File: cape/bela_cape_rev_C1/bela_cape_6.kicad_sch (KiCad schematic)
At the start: 48 parts, among them IC3 ES9080Q, IC8 TL974, IC9 TL974, J12 Conn_01x03, J13 Conn_01x03, J14 Conn_01x03, J15 Conn_01x03

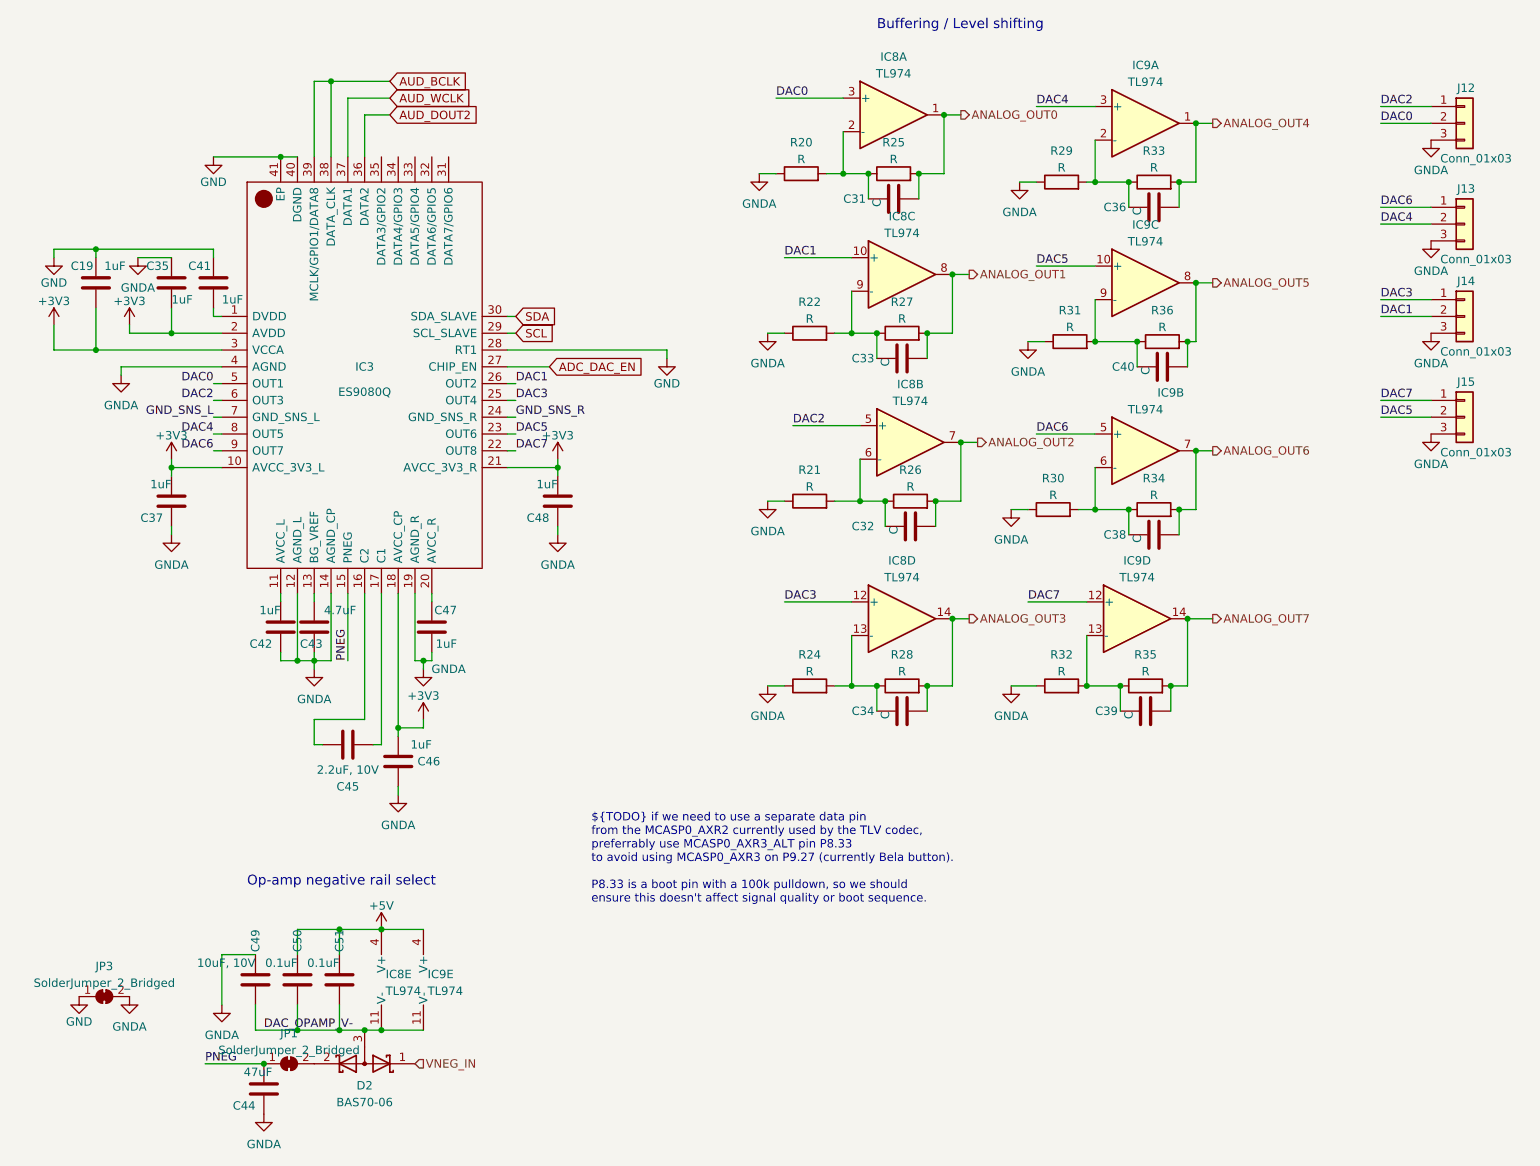
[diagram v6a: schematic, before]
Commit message: Bela cape C1: renumber components
(cherry picked from commit 6ebfe9c44bb7559ffb4c9dbd092e49803523e6a1)
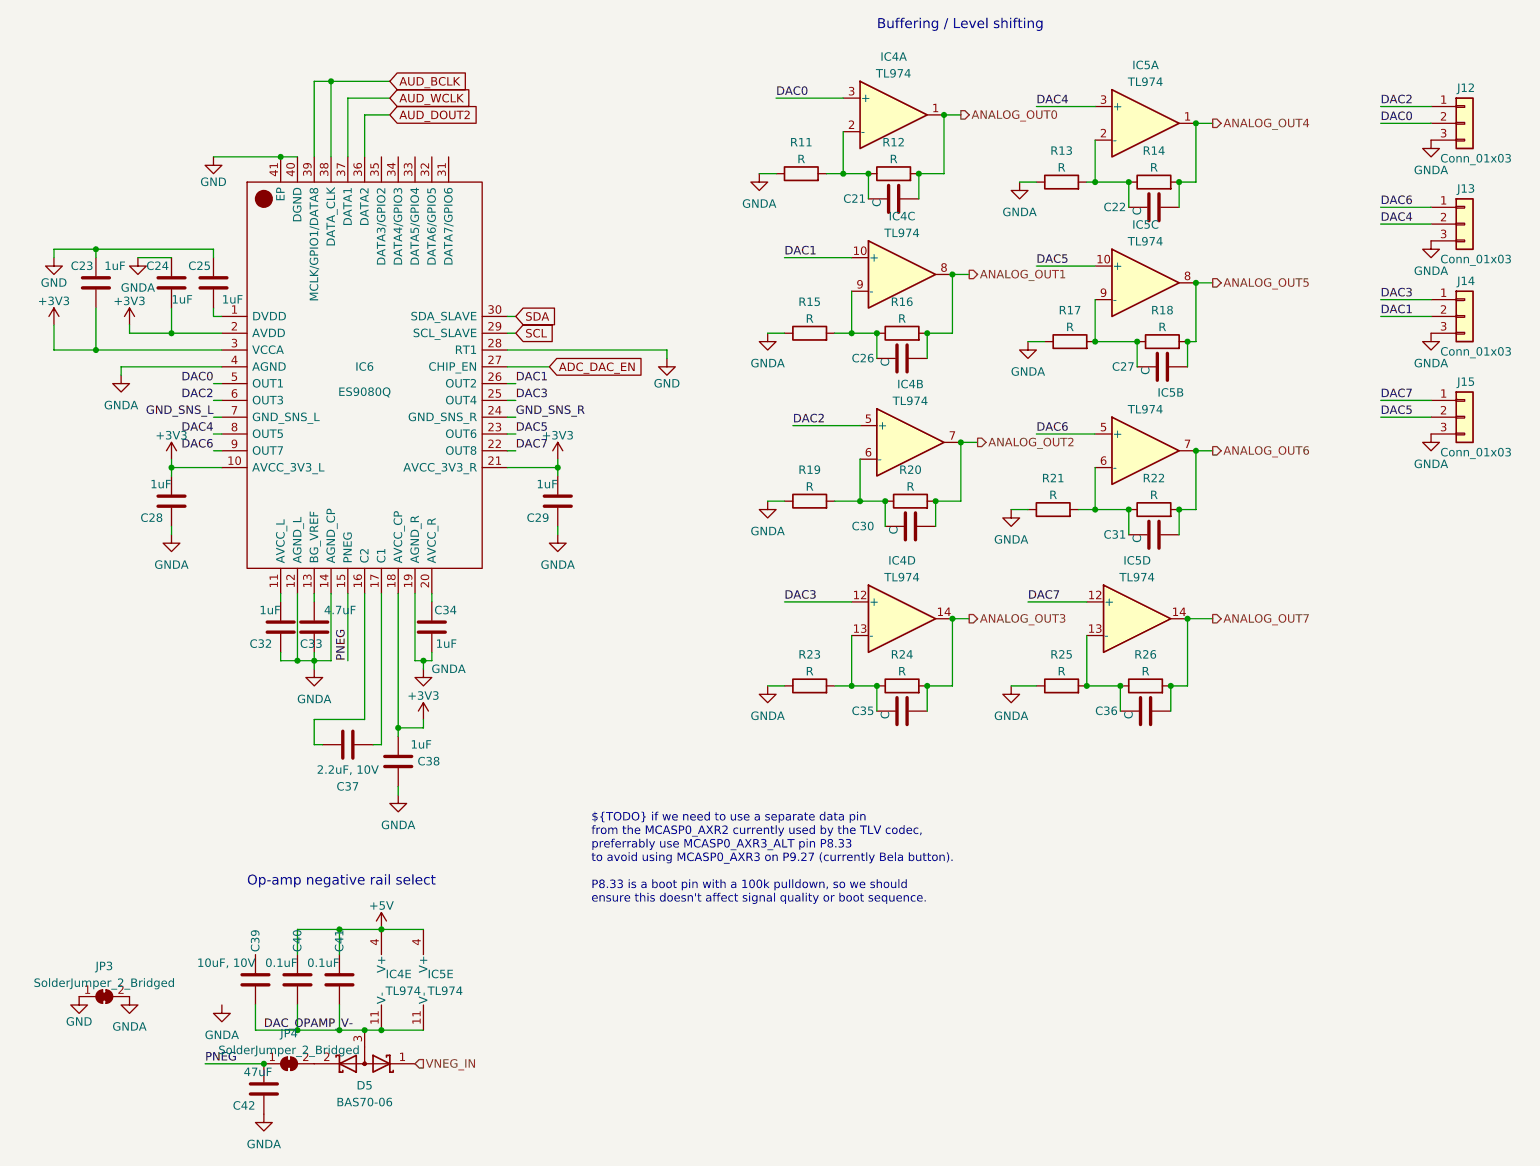
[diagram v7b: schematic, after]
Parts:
- renumbered C31 to C21, C36 to C22, C19 to C23, C35 to C24, C41 to C25, C33 to C26, C40 to C27, C37 to C28, C48 to C29, C32 to C30, C38 to C31, C42 to C32, C43 to C33, C47 to C34, C34 to C35, C39 to C36, C45 to C37, C46 to C38, C49 to C39, C50 to C40, C51 to C41, C44 to C42, D2 to D5, IC8 to IC4, IC9 to IC5, IC3 to IC6, JP1 to JP4, R20 to R11, R25 to R12, R29 to R13, R33 to R14, R22 to R15, R27 to R16, R31 to R17, R36 to R18, R21 to R19, R26 to R20, R30 to R21, R34 to R22, R24 to R23, R28 to R24, R32 to R25, R35 to R26
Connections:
- net GNDA: no longer C39.2

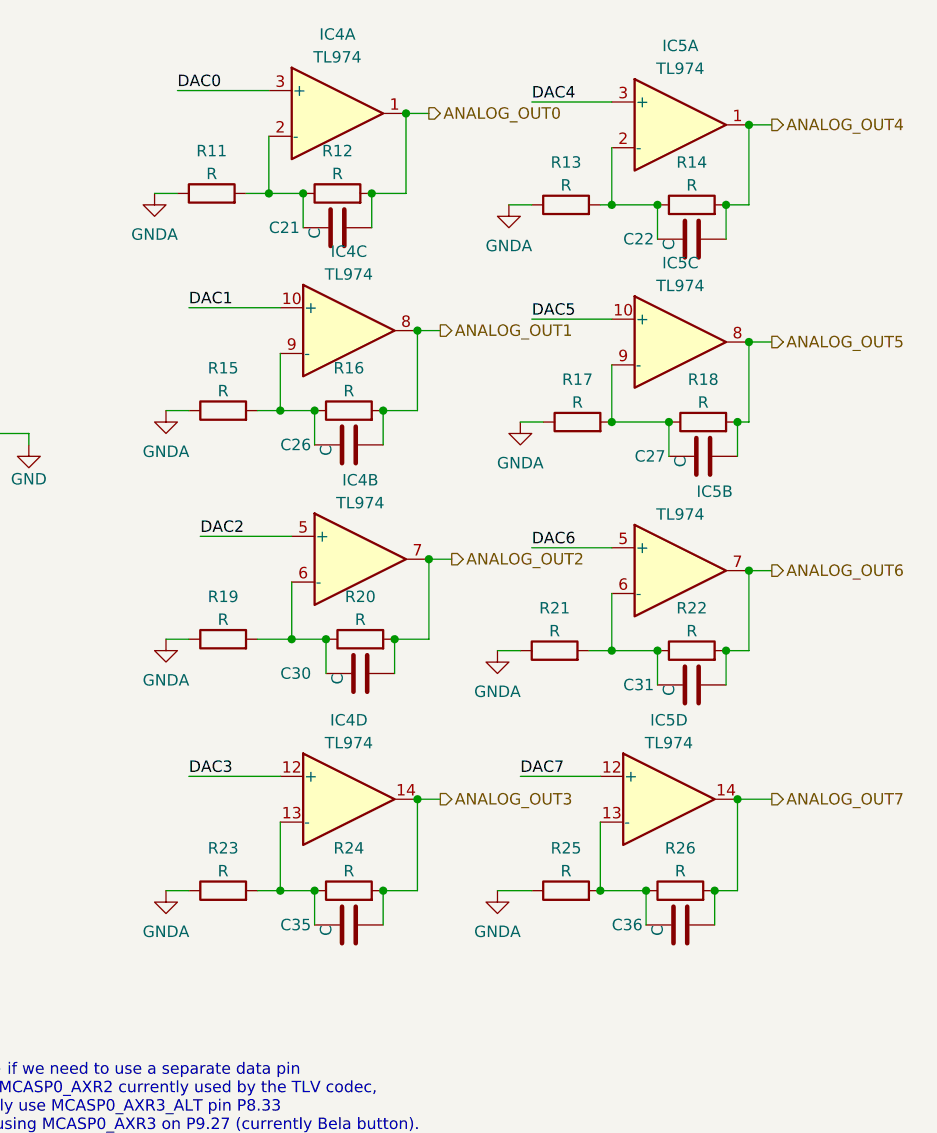
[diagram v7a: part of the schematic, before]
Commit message: First complete iteration of C1 cape layout
(cherry picked from commit 0ee733c70b42f416809330055e007cefcdb105fa)
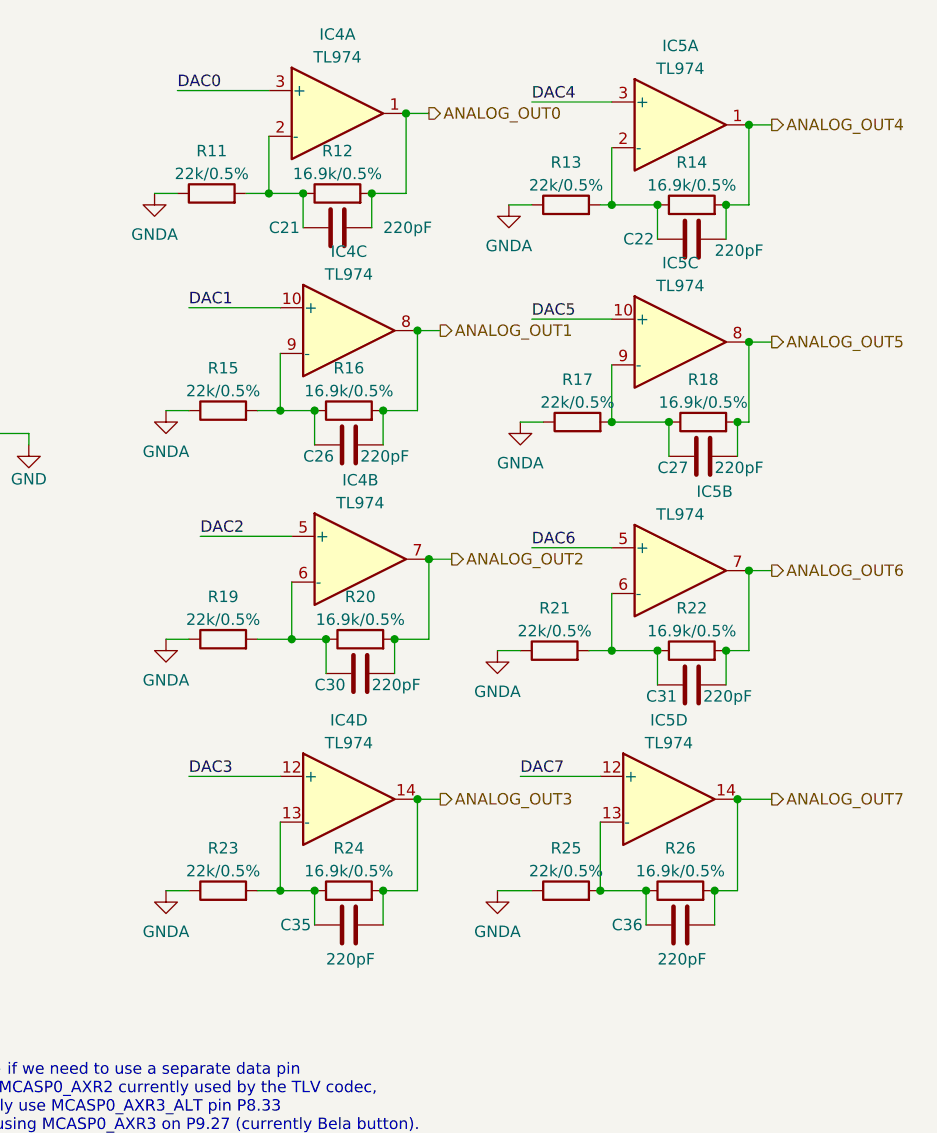
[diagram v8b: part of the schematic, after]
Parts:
- C21, C22, C26, C27, C30, C31, C35, C36: value C -> 220pF
- R11, R13, R15, R17, R19, R21, R23, R25: value R -> 22k/0.5%
- R12, R14, R16, R18, R20, R22, R24, R26: value R -> 16.9k/0.5%
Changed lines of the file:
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@@
   (symbol (lib_id "Device:C") (at 194.31 69.85 270) (unit 1)
     (in_bom yes) (on_board yes)
-    (property "Reference" "C27" (id 0) (at 186.69 69.85 90)
-      (effects (font (size 1.27 1.27)) (justify left))
-    )
-    (property "Value" "C" (id 1) (at 191.77 69.85 0)
+    (property "Reference" "C27" (id 0) (at 189.23 71.12 90)
+      (effects (font (size 1.27 1.27)) (justify left))
+    )
+    (property "Value" "220pF" (id 1) (at 195.58 71.12 90)
       (effects (font (size 1.27 1.27)) (justify left))
     )
@@
       (effects (font (size 1.27 1.27)) (justify left))
     )
-    (property "Value" "C" (id 1) (at 189.23 121.92 0)
+    (property "Value" "220pF" (id 1) (at 189.23 125.73 90)
       (effects (font (size 1.27 1.27)) (justify left))
     )
@@
     (in_bom yes) (on_board yes) (fields_autoplaced)
     (property "Reference" "R19" (id 0) (at 140.97 85.4542 90))
-    (property "Value" "R" (id 1) (at 140.97 87.9911 90))
+    (property "Value" "22k/0.5%" (id 1) (at 140.97 87.9911 90))
     (property "Footprint" "Resistor_SMD:R_0603_1608Metric" (id 2) (at 140.97 91.948 90)
       (effects (font (size 1.27 1.27)) hide)
@@
     (in_bom yes) (on_board yes) (fields_autoplaced)
     (property "Reference" "R26" (id 0) (at 191.77 113.3942 90))
-    (property "Value" "R" (id 1) (at 191.77 115.9311 90))
+    (property "Value" "16.9k/0.5%" (id 1) (at 191.77 115.9311 90))
     (property "Footprint" "Resistor_SMD:R_0603_1608Metric" (id 2) (at 191.77 119.888 90)
       (effects (font (size 1.27 1.27)) hide)
@@
     (in_bom yes) (on_board yes) (fields_autoplaced)
     (property "Reference" "R11" (id 0) (at 139.7 35.9242 90))
-    (property "Value" "R" (id 1) (at 139.7 38.4611 90))
+    (property "Value" "22k/0.5%" (id 1) (at 139.7 38.4611 90))
     (property "Footprint" "Resistor_SMD:R_0603_1608Metric" (id 2) (at 139.7 42.418 90)
       (effects (font (size 1.27 1.27)) hide)
@@
     (in_bom yes) (on_board yes) (fields_autoplaced)
     (property "Reference" "R24" (id 0) (at 154.94 113.3942 90))
-    (property "Value" "R" (id 1) (at 154.94 115.9311 90))
+    (property "Value" "16.9k/0.5%" (id 1) (at 154.94 115.9311 90))
     (property "Footprint" "Resistor_SMD:R_0603_1608Metric" (id 2) (at 154.94 119.888 90)
       (effects (font (size 1.27 1.27)) hide)
@@
     (in_bom yes) (on_board yes) (fields_autoplaced)
     (property "Reference" "R14" (id 0) (at 193.04 37.1942 90))
-    (property "Value" "R" (id 1) (at 193.04 39.7311 90))
+    (property "Value" "16.9k/0.5%" (id 1) (at 193.04 39.7311 90))
     (property "Footprint" "Resistor_SMD:R_0603_1608Metric" (id 2) (at 193.04 43.688 90)
       (effects (font (size 1.27 1.27)) hide)
@@
     (in_bom yes) (on_board yes) (fields_autoplaced)
     (property "Reference" "R22" (id 0) (at 193.04 86.7242 90))
-    (property "Value" "R" (id 1) (at 193.04 89.2611 90))
+    (property "Value" "16.9k/0.5%" (id 1) (at 193.04 89.2611 90))
     (property "Footprint" "Resistor_SMD:R_0603_1608Metric" (id 2) (at 193.04 93.218 90)
       (effects (font (size 1.27 1.27)) hide)
@@
   (symbol (lib_id "Device:C") (at 154.94 68.58 270) (unit 1)
     (in_bom yes) (on_board yes)
-    (property "Reference" "C26" (id 0) (at 147.32 68.58 90)
-      (effects (font (size 1.27 1.27)) (justify left))
-    )
-    (property "Value" "C" (id 1) (at 152.4 68.58 0)
+    (property "Reference" "C26" (id 0) (at 149.86 69.85 90)
+      (effects (font (size 1.27 1.27)) (justify left))
+    )
+    (property "Value" "220pF" (id 1) (at 156.21 69.85 90)
       (effects (font (size 1.27 1.27)) (justify left))
     )
@@
   (symbol (lib_id "Device:C") (at 193.04 95.25 270) (unit 1)
     (in_bom yes) (on_board yes)
-    (property "Reference" "C31" (id 0) (at 185.42 95.25 90)
-      (effects (font (size 1.27 1.27)) (justify left))
-    )
-    (property "Value" "C" (id 1) (at 190.5 95.25 0)
+    (property "Reference" "C31" (id 0) (at 187.96 96.52 90)
+      (effects (font (size 1.27 1.27)) (justify left))
+    )
+    (property "Value" "220pF" (id 1) (at 194.31 96.52 90)
       (effects (font (size 1.27 1.27)) (justify left))
     )
@@
   (symbol (lib_id "Device:C") (at 156.21 93.98 270) (unit 1)
     (in_bom yes) (on_board yes)
-    (property "Reference" "C30" (id 0) (at 147.32 93.98 90)
-      (effects (font (size 1.27 1.27)) (justify left))
-    )
-    (property "Value" "C" (id 1) (at 153.67 93.98 0)
+    (property "Reference" "C30" (id 0) (at 151.13 95.25 90)
+      (effects (font (size 1.27 1.27)) (justify left))
+    )
+    (property "Value" "220pF" (id 1) (at 157.48 95.25 90)
       (effects (font (size 1.27 1.27)) (justify left))
     )
@@
     (in_bom yes) (on_board yes) (fields_autoplaced)
     (property "Reference" "R18" (id 0) (at 194.31 61.3242 90))
-    (property "Value" "R" (id 1) (at 194.31 63.8611 90))
+    (property "Value" "16.9k/0.5%" (id 1) (at 194.31 63.8611 90))
     (property "Footprint" "Resistor_SMD:R_0603_1608Metric" (id 2) (at 194.31 67.818 90)
       (effects (font (size 1.27 1.27)) hide)
@@
     (in_bom yes) (on_board yes) (fields_autoplaced)
     (property "Reference" "R17" (id 0) (at 180.34 61.3242 90))
-    (property "Value" "R" (id 1) (at 180.34 63.8611 90))
+    (property "Value" "22k/0.5%" (id 1) (at 180.34 63.8611 90))
     (property "Footprint" "Resistor_SMD:R_0603_1608Metric" (id 2) (at 180.34 67.818 90)
       (effects (font (size 1.27 1.27)) hide)
@@
     (in_bom yes) (on_board yes) (fields_autoplaced)
     (property "Reference" "R25" (id 0) (at 179.07 113.3942 90))
-    (property "Value" "R" (id 1) (at 179.07 115.9311 90))
+    (property "Value" "22k/0.5%" (id 1) (at 179.07 115.9311 90))
     (property "Footprint" "Resistor_SMD:R_0603_1608Metric" (id 2) (at 179.07 119.888 90)
       (effects (font (size 1.27 1.27)) hide)
@@
     (in_bom yes) (on_board yes) (fields_autoplaced)
     (property "Reference" "R20" (id 0) (at 156.21 85.4542 90))
-    (property "Value" "R" (id 1) (at 156.21 87.9911 90))
+    (property "Value" "16.9k/0.5%" (id 1) (at 156.21 87.9911 90))
     (property "Footprint" "Resistor_SMD:R_0603_1608Metric" (id 2) (at 156.21 91.948 90)
       (effects (font (size 1.27 1.27)) hide)
@@
     (in_bom yes) (on_board yes) (fields_autoplaced)
     (property "Reference" "R12" (id 0) (at 153.67 35.9242 90))
-    (property "Value" "R" (id 1) (at 153.67 38.4611 90))
+    (property "Value" "16.9k/0.5%" (id 1) (at 153.67 38.4611 90))
     (property "Footprint" "Resistor_SMD:R_0603_1608Metric" (id 2) (at 153.67 42.418 90)
       (effects (font (size 1.27 1.27)) hide)
@@
       (effects (font (size 1.27 1.27)) (justify left))
     )
-    (property "Value" "C" (id 1) (at 151.13 44.45 0)
+    (property "Value" "220pF" (id 1) (at 158.75 44.45 90)
       (effects (font (size 1.27 1.27)) (justify left))
     )
@@
     (in_bom yes) (on_board yes) (fields_autoplaced)
     (property "Reference" "R21" (id 0) (at 177.8 86.7242 90))
-    (property "Value" "R" (id 1) (at 177.8 89.2611 90))
+    (property "Value" "22k/0.5%" (id 1) (at 177.8 89.2611 90))
     (property "Footprint" "Resistor_SMD:R_0603_1608Metric" (id 2) (at 177.8 93.218 90)
       (effects (font (size 1.27 1.27)) hide)
@@
       (effects (font (size 1.27 1.27)) (justify left))
     )
-    (property "Value" "C" (id 1) (at 152.4 121.92 0)
+    (property "Value" "220pF" (id 1) (at 152.4 125.73 90)
       (effects (font (size 1.27 1.27)) (justify left))
     )
@@
     (in_bom yes) (on_board yes) (fields_autoplaced)
     (property "Reference" "R15" (id 0) (at 140.97 60.0542 90))
-    (property "Value" "R" (id 1) (at 140.97 62.5911 90))
+    (property "Value" "22k/0.5%" (id 1) (at 140.97 62.5911 90))
     (property "Footprint" "Resistor_SMD:R_0603_1608Metric" (id 2) (at 140.97 66.548 90)
       (effects (font (size 1.27 1.27)) hide)
@@
     (in_bom yes) (on_board yes) (fields_autoplaced)
     (property "Reference" "R23" (id 0) (at 140.97 113.3942 90))
-    (property "Value" "R" (id 1) (at 140.97 115.9311 90))
+    (property "Value" "22k/0.5%" (id 1) (at 140.97 115.9311 90))
     (property "Footprint" "Resistor_SMD:R_0603_1608Metric" (id 2) (at 140.97 119.888 90)
       (effects (font (size 1.27 1.27)) hide)
@@
       (effects (font (size 1.27 1.27)) (justify left))
     )
-    (property "Value" "C" (id 1) (at 190.5 45.72 0)
+    (property "Value" "220pF" (id 1) (at 195.58 46.99 90)
       (effects (font (size 1.27 1.27)) (justify left))
     )
@@
     (in_bom yes) (on_board yes) (fields_autoplaced)
     (property "Reference" "R13" (id 0) (at 179.07 37.1942 90))
-    (property "Value" "R" (id 1) (at 179.07 39.7311 90))
+    (property "Value" "22k/0.5%" (id 1) (at 179.07 39.7311 90))
     (property "Footprint" "Resistor_SMD:R_0603_1608Metric" (id 2) (at 179.07 43.688 90)
       (effects (font (size 1.27 1.27)) hide)
@@
     (in_bom yes) (on_board yes) (fields_autoplaced)
     (property "Reference" "R16" (id 0) (at 154.94 60.0542 90))
-    (property "Value" "R" (id 1) (at 154.94 62.5911 90))
+    (property "Value" "16.9k/0.5%" (id 1) (at 154.94 62.5911 90))
     (property "Footprint" "Resistor_SMD:R_0603_1608Metric" (id 2) (at 154.94 66.548 90)
       (effects (font (size 1.27 1.27)) hide)
@@
   )
   (symbol (lib_id "Amplifier_Operational:TL074") (at 154.94 55.88 0) (unit 3)
-    (in_bom yes) (on_board yes) (fields_autoplaced)
+    (in_bom yes) (on_board yes)
     (property "Reference" "IC4" (id 0) (at 154.94 47.1002 0))
     (property "Value" "TL974" (id 1) (at 154.94 49.6371 0))
